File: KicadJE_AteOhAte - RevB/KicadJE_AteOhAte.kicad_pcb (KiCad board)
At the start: 2 copper layers, 100 x 100 mm, 326 parts, among them J201 In_Accent, J202 In Gate, J203 Out Tom, J301 Noise_In, J302 In_Accent, J303 In Gate, J304 Out Tom, P201 Doepfer_Power_10pin, P301 Doepfer_Power_10pin, Q201 MMBT2222A, Q202 MMBT2222A, Q203 MMBT2222A, Q204 MMBT2222A, Q205 MMBT2907A, Q206 MMBT2222A, Q207 MMBT2222A, Q301 MMBT2222A, Q302 MMBT2222A, Q303 MMBT2222A, Q304 MMBT2907A, Q305 MMBT2222A, Q306 MMBT2222A, SW201 Con/Tom, SW301 Con/Tom, U201 TL072, U202 TL072, U203 TL072, U301 TL072, U302 TL072

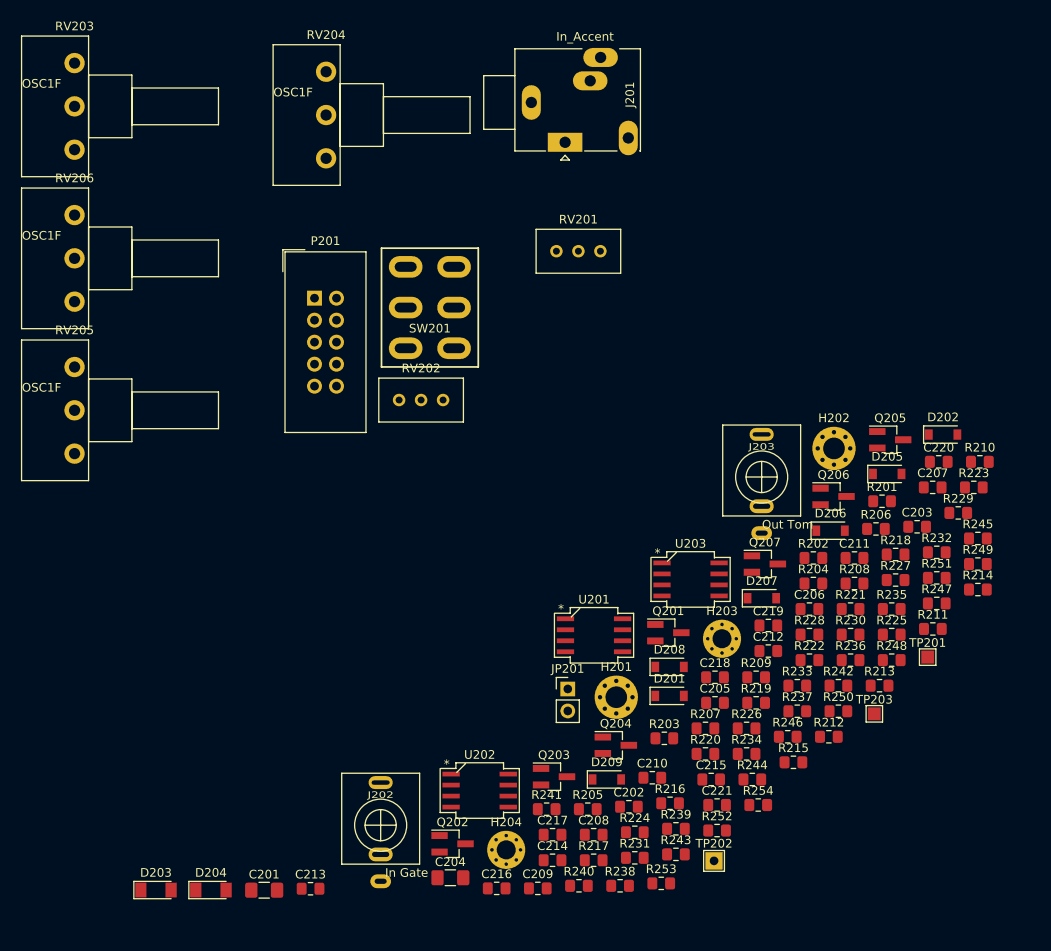
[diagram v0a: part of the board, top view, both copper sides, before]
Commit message: remove excess components
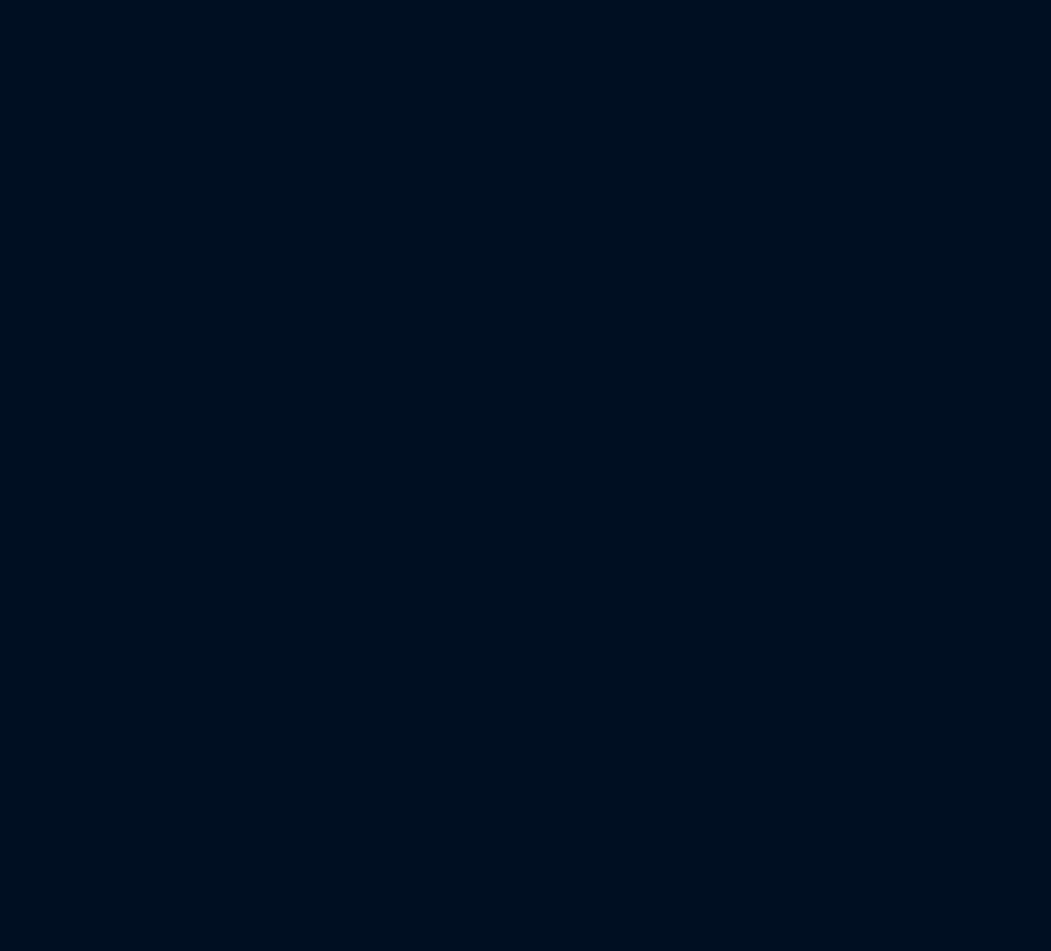
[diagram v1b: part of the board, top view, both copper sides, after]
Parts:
- removed the C201 at (-16.8, 7.80)
- removed the C202 at (25.3, -1.84)
- removed the C203 at (58.6, -34.2)
- removed the C204 at (4.68, 6.36)
- removed the C205 at (35.2, -13.8)
- removed the C206 at (46.1, -24.7)
- removed the C207 at (60.4, -38.7)
- removed the C208 at (21.2, 1.39)
- removed the C209 at (14.8, 7.59)
- removed the C210 at (28.0, -5.19)
- removed the C211 at (51.3, -30.6)
- removed the C212 at (41.4, -19.8)
- removed the C213 at (-11.5, 7.63)
- removed the C214 at (16.5, 4.34)
- removed the C215 at (34.8, -4.99)
- removed the C216 at (10.0, 7.59)
- removed the C217 at (16.5, 1.39)
- removed the C218 at (35.2, -16.8)
- removed the C219 at (41.4, -22.8)
- removed the C220 at (61.1, -41.7)
- removed the C221 at (35.5, -2.04)
- removed the D201 at (30.0, -14.6)
- removed the D202 at (61.6, -44.8)
- removed the D203 at (-29.3, 7.78)
- removed the D204 at (-23.0, 7.78)
- removed the D205 at (55.1, -40.3)
- removed the D206 at (48.6, -33.7)
- removed the D207 at (40.6, -25.9)
- removed the D208 at (30.0, -18.0)
- removed the D209 at (22.7, -4.99)
- removed H201, H202: 2,5mm, MountingHole:MountingHole_2.5mm_Pad_Via
- removed H203: 2,2mm, MountingHole:MountingHole_2.2mm_M2_Pad_Via
- removed the H204 at (11.1, 3.14)
- removed the J201 at (17.9, -78.6)
- removed the J202 at (-3.37, 0.29)
- removed the J203 at (40.6, -39.9)
- removed the JP201 at (18.2, -15.4)
- removed the P201 at (-11.0, -60.6)
- removed the Q201 at (29.8, -21.9)
- removed the Q202 at (4.93, 2.44)
- removed the Q203 at (16.6, -5.31)
- removed the Q204 at (23.8, -8.94)
- removed the Q205 at (55.5, -44.2)
- removed the Q206 at (48.9, -37.7)
- removed the Q207 at (41.0, -29.9)
- removed the R201 at (54.5, -37.1)
- removed the R202 at (46.6, -30.6)
- removed the R203 at (29.4, -9.74)
- removed the R204 at (46.6, -27.6)
- removed the R205 at (20.5, -1.56)
- removed the R206 at (53.8, -33.9)
- removed the R207 at (34.1, -10.9)
- removed the R208 at (51.3, -27.6)
- removed the R209 at (40.0, -16.8)
- removed the R210 at (65.8, -41.7)
- removed the R211 at (60.4, -22.4)
- removed the R212 at (48.4, -9.92)
- removed the R213 at (54.2, -15.8)
- removed the R214 at (65.6, -26.9)
- removed the R215 at (44.3, -6.97)
- removed the R216 at (30.0, -2.24)
- removed the R217 at (21.2, 4.34)
- removed the R218 at (56.1, -31.0)
- removed the R219 at (40.0, -13.8)
- removed the R220 at (34.1, -7.94)
- removed the R221 at (50.9, -24.7)
- removed the R222 at (46.1, -18.8)
- removed the R223 at (65.1, -38.7)
- removed the R224 at (26.0, 1.11)
- removed the R225 at (55.6, -21.7)
- removed the R226 at (38.9, -10.9)
- removed the R227 at (56.1, -28.0)
- removed the R228 at (46.1, -21.7)
- removed the R229 at (63.3, -35.8)
- removed the R230 at (50.9, -21.7)
- removed the R231 at (26.0, 4.06)
- removed the R232 at (60.8, -31.2)
- removed the R233 at (44.7, -15.8)
- removed the R234 at (38.9, -7.94)
- removed the R235 at (55.6, -24.7)
- removed the R236 at (50.9, -18.8)
- removed the R237 at (44.7, -12.9)
- removed the R238 at (24.3, 7.29)
- removed the R239 at (30.7, 0.71)
- removed the R240 at (19.5, 7.29)
- removed the R241 at (15.8, -1.56)
- removed the R242 at (49.5, -15.8)
- removed the R243 at (30.7, 3.66)
- removed the R244 at (39.5, -4.99)
- removed the R245 at (65.6, -32.8)
- removed the R246 at (43.6, -9.92)
- removed the R247 at (60.8, -25.3)
- removed the R248 at (55.6, -18.8)
- removed the R249 at (65.6, -29.9)
- removed the R250 at (49.5, -12.9)
- removed the R251 at (60.8, -28.3)
- removed the R252 at (35.5, 0.91)
- removed the R253 at (29.0, 7.01)
- removed the R254 at (40.2, -2.04)
- removed the RV201 at (22.0, -66.0)
- removed the RV202 at (3.84, -48.8)
- removed the RV203 at (-38.7, -77.7)
- removed the RV204 at (-9.67, -76.7)
- removed the RV205 at (-38.7, -42.6)
- removed the RV206 at (-38.7, -60.2)
- removed the SW201 at (2.31, -59.5)
- removed the TP201 at (59.8, -19.1)
- removed the TP202 at (35.1, 4.41)
- removed the TP203 at (53.6, -12.6)
- removed the U201 at (21.3, -21.6)
- removed the U202 at (8.07, -3.71)
- removed the U203 at (32.4, -28.1)
